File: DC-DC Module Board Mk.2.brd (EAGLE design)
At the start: 177.9 x 101.7 mm, 159 parts, among them Q1 FDN340P, U2 AP1117_LIN_REG, U3 LM1085IS-5.0

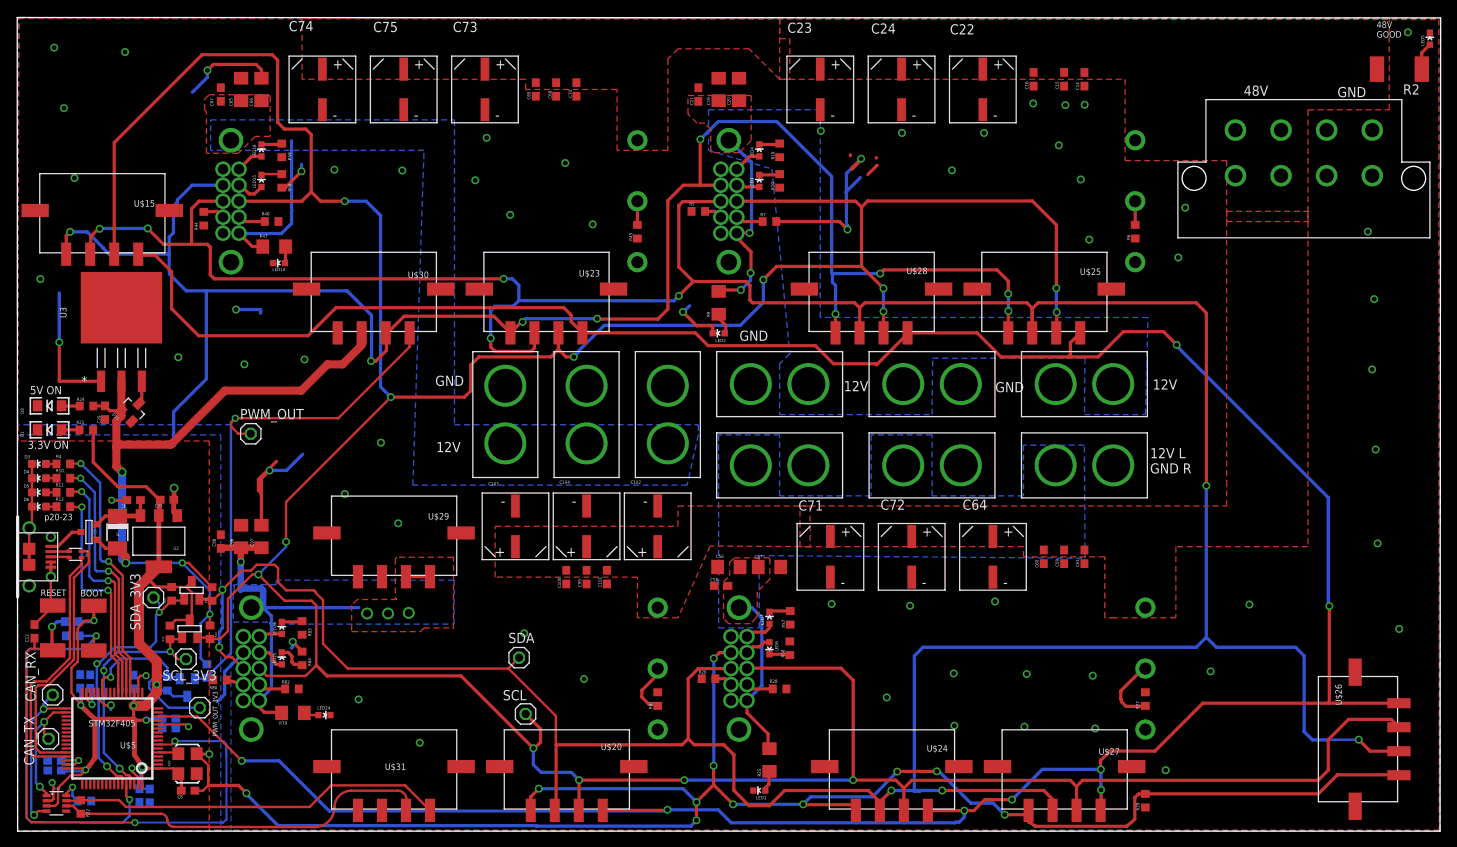
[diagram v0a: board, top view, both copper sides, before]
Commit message: refixed restring options, redrew curvy trace
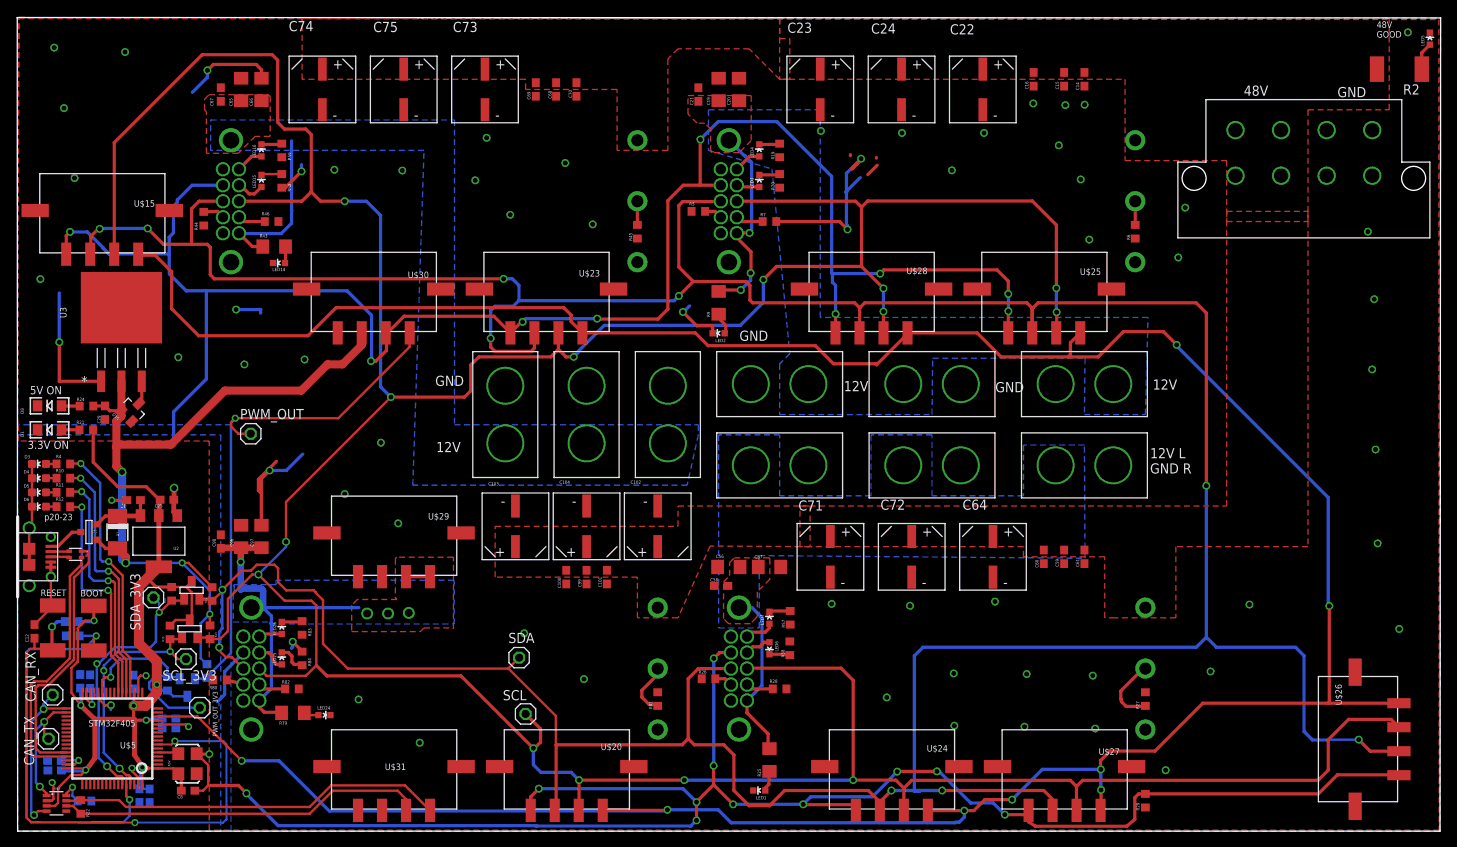
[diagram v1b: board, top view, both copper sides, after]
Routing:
- net CANL: track 47.3 -> 46.0 mm
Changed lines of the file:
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@@
 </class>
 </classes>
-<designrules name="typical_4pcb">
+<designrules name="typical_4pcb *">
 <description language="de">&lt;b&gt;EAGLE Design Rules&lt;/b&gt;
 &lt;p&gt;
@@
 <param name="msMicroVia" value="9.98981875mm"/>
 <param name="msBlindViaRatio" value="0.5"/>
-<param name="rvPadTop" value="0.25"/>
-<param name="rvPadInner" value="0.25"/>
-<param name="rvPadBottom" value="0.25"/>
+<param name="rvPadTop" value="0"/>
+<param name="rvPadInner" value="0"/>
+<param name="rvPadBottom" value="0"/>
 <param name="rvViaOuter" value="0.25"/>
 <param name="rvViaInner" value="0.25"/>
@@
 <wire x1="6.0764" y1="1.8848" x2="6.9172" y2="1.8848" width="0.3048" layer="1"/>
 <wire x1="6.9172" y1="1.8848" x2="7.8994" y2="0.9026" width="0.3048" layer="1"/>
-<wire x1="7.8994" y1="0.9026" x2="17.8934" y2="0.9026" width="0.3048" layer="1"/>
-<wire x1="41.7068" y1="3.7846" x2="47.498" y2="3.7846" width="0.3048" layer="1"/>
-<wire x1="19.583315625" y1="-0.737890625" x2="34.7472" y2="-0.762" width="0.3048" layer="1"/>
-<wire x1="17.8934" y1="0.9026" x2="18.7198" y2="0.0762" width="0.3048" layer="1" curve="-90"/>
-<wire x1="18.7198" y1="0.0762" x2="19.533890625" y2="-0.737890625" width="0.3048" layer="1" curve="90"/>
-<wire x1="19.533890625" y1="-0.737890625" x2="19.583315625" y2="-0.737890625" width="0.3048" layer="1"/>
-<wire x1="34.7472" y1="-0.762" x2="37.1602" y2="-0.762" width="0.3048" layer="1"/>
-<wire x1="37.1602" y1="-0.762" x2="39.5986" y2="1.6764" width="0.3048" layer="1" curve="90"/>
-<wire x1="39.5986" y1="1.6764" x2="41.7068" y2="3.7846" width="0.3048" layer="1" curve="-90"/>
-<wire x1="47.498" y1="3.7846" x2="48.6156" y2="2.667" width="0.3048" layer="1" curve="-90"/>
+<wire x1="39.3846" y1="3.7846" x2="47.498" y2="3.7846" width="0.3048" layer="1"/>
 <wire x1="48.6156" y1="2.667" x2="48.6156" y2="1.3906" width="0.3048" layer="1"/>
 <wire x1="48.6156" y1="1.3906" x2="48.55" y2="1.325" width="0.3048" layer="1" curve="-90"/>
+<wire x1="48.6156" y1="2.667" x2="47.498" y2="3.7846" width="0.3048" layer="1"/>
+<wire x1="39.3846" y1="3.7846" x2="36.5026" y2="0.9026" width="0.3048" layer="1"/>
+<wire x1="36.5026" y1="0.9026" x2="7.8994" y2="0.9026" width="0.3048" layer="1"/>
 </signal>
 <signal name="CANH">

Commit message: Cleaned up the board layout
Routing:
- net SDA1: track 35.2 -> 34.7 mm, vias 3 -> 2
- net SCL1: vias 3 -> 2
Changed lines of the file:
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@@
 <?xml version="1.0" encoding="utf-8"?>
 <!DOCTYPE eagle SYSTEM "eagle.dtd">
-<eagle version="7.4.0">
+<eagle version="7.5.0">
 <drawing>
 <settings>
@@
 <setting verticaltext="up"/>
 </settings>
-<grid distance="0.01" unitdist="mm" unit="mm" style="lines" multiple="1" display="yes" altdistance="0.01" altunitdist="mm" altunit="mm"/>
+<grid distance="0.393700787" unitdist="mil" unit="mil" style="lines" multiple="1" display="yes" altdistance="0.01" altunitdist="mm" altunit="mm"/>
 <layers>
 <layer number="1" name="Top" color="4" fill="1" visible="yes" active="yes"/>
@@
 <contactref element="R11" pad="2"/>
 <wire x1="13.0864" y1="16.0624" x2="13.0864" y2="19.959" width="0.3048" layer="1"/>
-<wire x1="13.0864" y1="19.959" x2="12.1666" y2="20.8788" width="0.3048" layer="1"/>
-<wire x1="12.1666" y1="20.8788" x2="12.1666" y2="29.7434" width="0.3048" layer="1"/>
+<wire x1="13.0864" y1="19.959" x2="12.1666" y2="20.8588" width="0.3048" layer="1"/>
+<wire x1="12.1666" y1="20.8588" x2="12.1666" y2="29.7434" width="0.3048" layer="1"/>
 <wire x1="12.1666" y1="29.7434" x2="11.9634" y2="29.9466" width="0.3048" layer="1"/>
 <wire x1="11.9634" y1="29.9466" x2="11.3284" y2="30.0228" width="0.3048" layer="1"/>
@@
 <contactref element="U$9" pad="3"/>
 <contactref element="R16" pad="1"/>
-<via x="9.906" y="19.6596" extent="1-16" drill="0.508"/>
 <wire x1="19.2532" y1="27.5472" x2="20.636" y2="27.5472" width="0.3048" layer="1"/>
 <wire x1="20.636" y1="27.5472" x2="20.8178" y2="27.729" width="0.3048" layer="1"/>
-<wire x1="17.2974" y1="22.4282" x2="17.2974" y2="25.6794" width="0.3048" layer="16"/>
+<wire x1="17.2874" y1="22.3882" x2="17.2974" y2="25.6794" width="0.3048" layer="16"/>
 <wire x1="17.2974" y1="25.6794" x2="17.7038" y2="26.0858" width="0.3048" layer="16"/>
 <via x="17.7038" y="26.0858" extent="1-16" drill="0.508"/>
 <wire x1="17.7038" y1="26.0858" x2="17.7918" y2="26.0858" width="0.3048" layer="1"/>
 <wire x1="17.7918" y1="26.0858" x2="19.2532" y2="27.5472" width="0.3048" layer="1"/>
-<wire x1="10.1092" y1="19.6596" x2="10.1981" y2="19.7485" width="0.3048" layer="16"/>
-<wire x1="10.1981" y1="19.7485" x2="12.1666" y2="21.717" width="0.3048" layer="16"/>
-<wire x1="12.1666" y1="21.717" x2="16.5862" y2="21.717" width="0.3048" layer="16"/>
-<wire x1="16.5862" y1="21.717" x2="17.2974" y2="22.4282" width="0.3048" layer="16"/>
+<wire x1="12.1666" y1="21.667" x2="16.5562" y2="21.657" width="0.3048" layer="16"/>
+<wire x1="16.5562" y1="21.657" x2="17.2874" y2="22.3882" width="0.3048" layer="16"/>
 <contactref element="U$5" pad="59"/>
 <via x="11.176" y="6.8326" extent="1-16" drill="0.6"/>
 <wire x1="11.176" y1="6.8326" x2="10.1346" y2="7.874" width="0.3048" layer="16"/>
-<wire x1="10.1346" y1="7.874" x2="10.1346" y2="15.4178" width="0.3048" layer="16"/>
-<wire x1="10.1346" y1="15.4178" x2="9.906" y2="15.6464" width="0.3048" layer="16"/>
-<wire x1="9.906" y1="15.6464" x2="9.906" y2="19.6596" width="0.3048" layer="16"/>
-<wire x1="9.906" y1="19.6596" x2="10.1981" y2="19.6596" width="0.3048" layer="16"/>
-<wire x1="10.1981" y1="19.6596" x2="10.1981" y2="19.7485" width="0.3048" layer="16"/>
 <wire x1="13.0864" y1="4.5624" x2="13.0864" y2="5.481" width="0.3048" layer="1"/>
 <wire x1="13.0864" y1="5.481" x2="12.954" y2="5.6134" width="0.3048" layer="1"/>
@@
 <wire x1="16.98" y1="27.93" x2="17.7038" y2="27.2062" width="0.254" layer="16"/>
 <wire x1="17.7038" y1="27.2062" x2="17.7038" y2="26.0858" width="0.254" layer="16"/>
+<wire x1="10.1346" y1="7.874" x2="10.1346" y2="19.6342" width="0.3048" layer="16"/>
+<wire x1="12.1666" y1="21.667" x2="12.1666" y2="21.6662" width="0.3048" layer="16"/>
+<wire x1="12.1666" y1="21.6662" x2="10.1346" y2="19.6342" width="0.3048" layer="16"/>
 </signal>
 <signal name="SCL1">
 <contactref element="BSS138" pad="3"/>
 <contactref element="R15" pad="1"/>
-<via x="10.7696" y="18.796" extent="1-16" drill="0.508"/>
 <wire x1="19.05" y1="22.7212" x2="19.1906" y2="22.7212" width="0.3048" layer="1"/>
 <wire x1="19.1906" y1="22.7212" x2="19.2024" y2="22.733" width="0.3048" layer="1"/>
@@
 <wire x1="19.0754" y1="21.1836" x2="19.0754" y2="22.6958" width="0.3048" layer="1"/>
 <wire x1="19.0754" y1="22.6958" x2="19.05" y2="22.7212" width="0.3048" layer="1"/>
-<wire x1="10.7696" y1="18.796" x2="10.7696" y2="19.4056" width="0.3048" layer="16"/>
 <wire x1="10.7696" y1="19.4056" x2="12.4968" y2="21.1328" width="0.3048" layer="16"/>
 <wire x1="12.4968" y1="21.1328" x2="19.0246" y2="21.1328" width="0.3048" layer="16"/>
@@
 <via x="12.7508" y="6.5532" extent="1-16" drill="0.6"/>
 <wire x1="12.7508" y1="6.5532" x2="10.7696" y2="8.5344" width="0.3048" layer="16"/>
-<wire x1="10.7696" y1="8.5344" x2="10.7696" y2="18.796" width="0.3048" layer="16"/>
+<wire x1="10.7696" y1="8.5344" x2="10.7696" y2="19.4056" width="0.3048" layer="16"/>
 <wire x1="14.0864" y1="5.5478" x2="13.9192" y2="5.715" width="0.3048" layer="1"/>
 <wire x1="13.9192" y1="5.715" x2="13.589" y2="5.715" width="0.3048" layer="1"/>

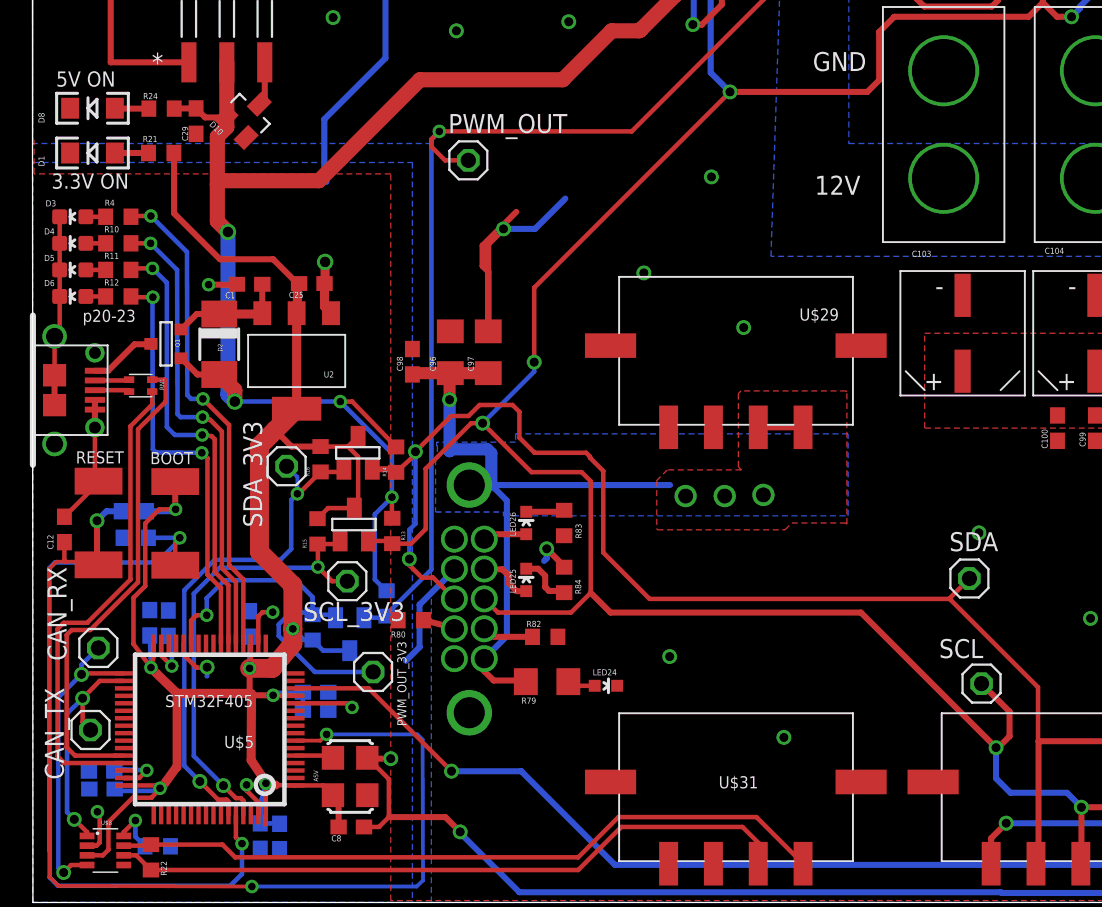
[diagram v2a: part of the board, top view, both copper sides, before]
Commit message: moved sda/scl pins and header pins
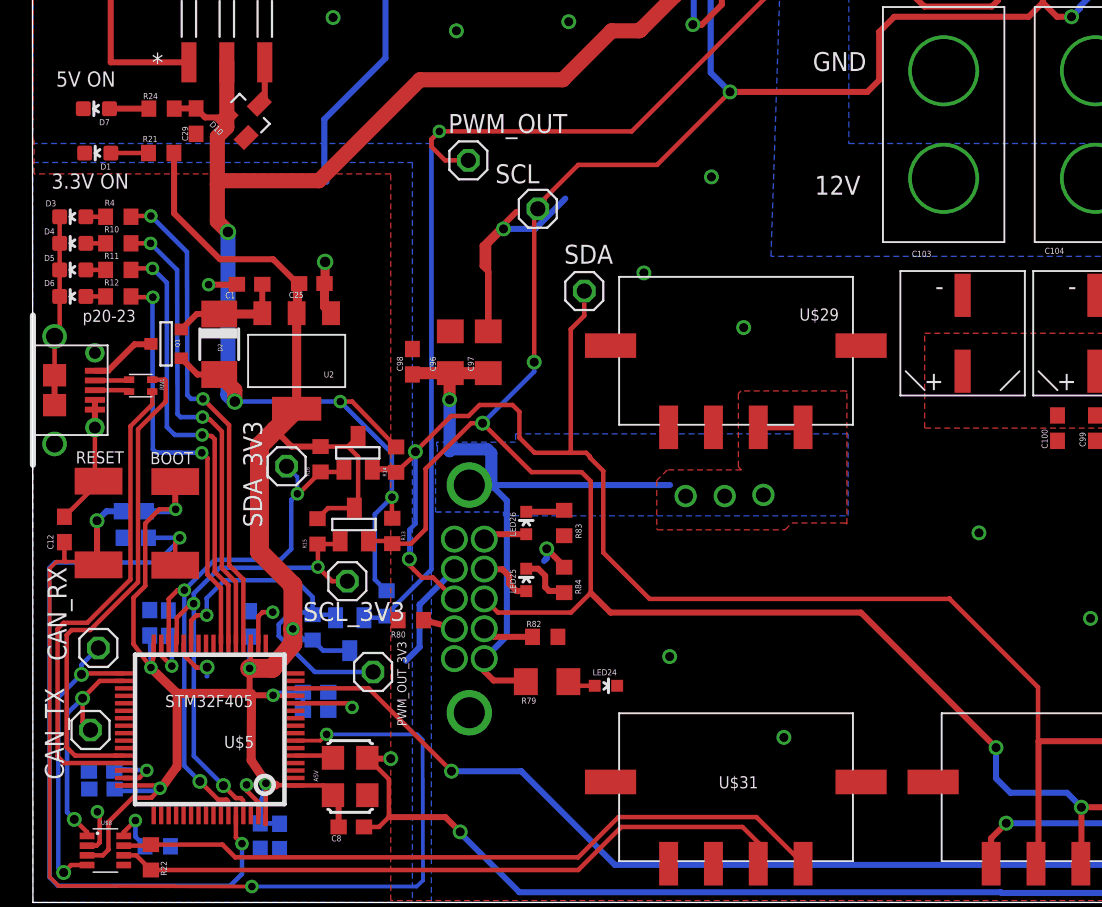
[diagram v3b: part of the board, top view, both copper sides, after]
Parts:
- removed D8: WHITE, SparkFun-LED:LED-1206
- added D7: RED, SparkFun-LED:LED-0603
- D1: value WHITE -> RED; device SparkFun-LED:LED-1206 -> SparkFun-LED:LED-0603
- moved SCL 43.5 mm to (33.8, 45.2)
- moved SDA 32.2 mm to (36.9, 39.7)
- moved D1 0.35 mm to (4.34, 48.9), turned to 90 degrees
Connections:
- removed net PB10: U$5.29
- removed net PB11: U$5.30
- new net PB7: U$5.59
- new net PB8: U$5.61
- net GND: now also D7.C; no longer D8.C
- net N$22: now also D7.A; no longer D8.A
- net SCL1: now also U$5.29; no longer U$5.61
- net SDA1: now also U$5.30; no longer U$5.59
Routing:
- net SDA: track 506.5 -> 515.9 mm
- net SDA1: track 34.7 -> 38.1 mm, vias 2 -> 3
- net SCL1: track 31.1 -> 33.4 mm, vias 2 -> 3
- net SCL: track 504.8 -> 504.1 mm

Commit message: more little fixes
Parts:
- moved SDA 1.25 mm to (36.1, 40.6)
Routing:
- net SDA: track 515.9 -> 516.5 mm
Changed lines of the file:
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@@
 <layer number="26" name="bNames" color="7" fill="1" visible="yes" active="yes"/>
 <layer number="27" name="tValues" color="7" fill="1" visible="yes" active="yes"/>
-<layer number="28" name="bValues" color="7" fill="1" visible="no" active="yes"/>
+<layer number="28" name="bValues" color="7" fill="1" visible="yes" active="yes"/>
 <layer number="29" name="tStop" color="7" fill="3" visible="no" active="yes"/>
 <layer number="30" name="bStop" color="7" fill="6" visible="no" active="yes"/>
@@
 <attribute name="VALUE" x="19.775" y="17.06" size="1.27" layer="27"/>
 </element>
-<element name="SDA" library="pinhead" package="1X01" value="" x="36.905" y="39.655"/>
+<element name="SDA" library="pinhead" package="1X01" value="" x="36.085" y="40.605"/>
 <element name="SCL" library="pinhead" package="1X01" value="" x="33.795" y="45.16" smashed="yes">
 <attribute name="NAME" x="30.9488" y="46.8688" size="1.27" layer="25" ratio="10"/>
@@
 <contactref element="SDA" pad="1"/>
 <wire x1="61.361" y1="19.091" x2="61.361" y2="19.05" width="0.3048" layer="1"/>
-<wire x1="36.905" y1="39.655" x2="36.905" y2="38.005" width="0.3048" layer="1"/>
-<wire x1="36.905" y1="38.005" x2="36" y2="37.1" width="0.3048" layer="1"/>
-<wire x1="36" y1="37.1" x2="36" y2="28.889" width="0.3048" layer="1"/>
+<wire x1="36" y1="40.52" x2="36" y2="28.889" width="0.3048" layer="1"/>
 <wire x1="36" y1="28.889" x2="36.06" y2="28.829" width="0.3048" layer="1"/>
+<wire x1="36" y1="40.52" x2="36.085" y2="40.605" width="0.3048" layer="1"/>
 </signal>
 <signal name="ALERT">
